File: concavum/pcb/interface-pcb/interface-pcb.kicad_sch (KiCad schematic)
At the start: 19 parts, among them J1 USB_C_Port, J2 Audio_Jack, J3 ISP_pads, J4 FPC_connector, U1 ATmega32U4-A, U2 MCP23017_SO, Y1 Crystal_16MHz

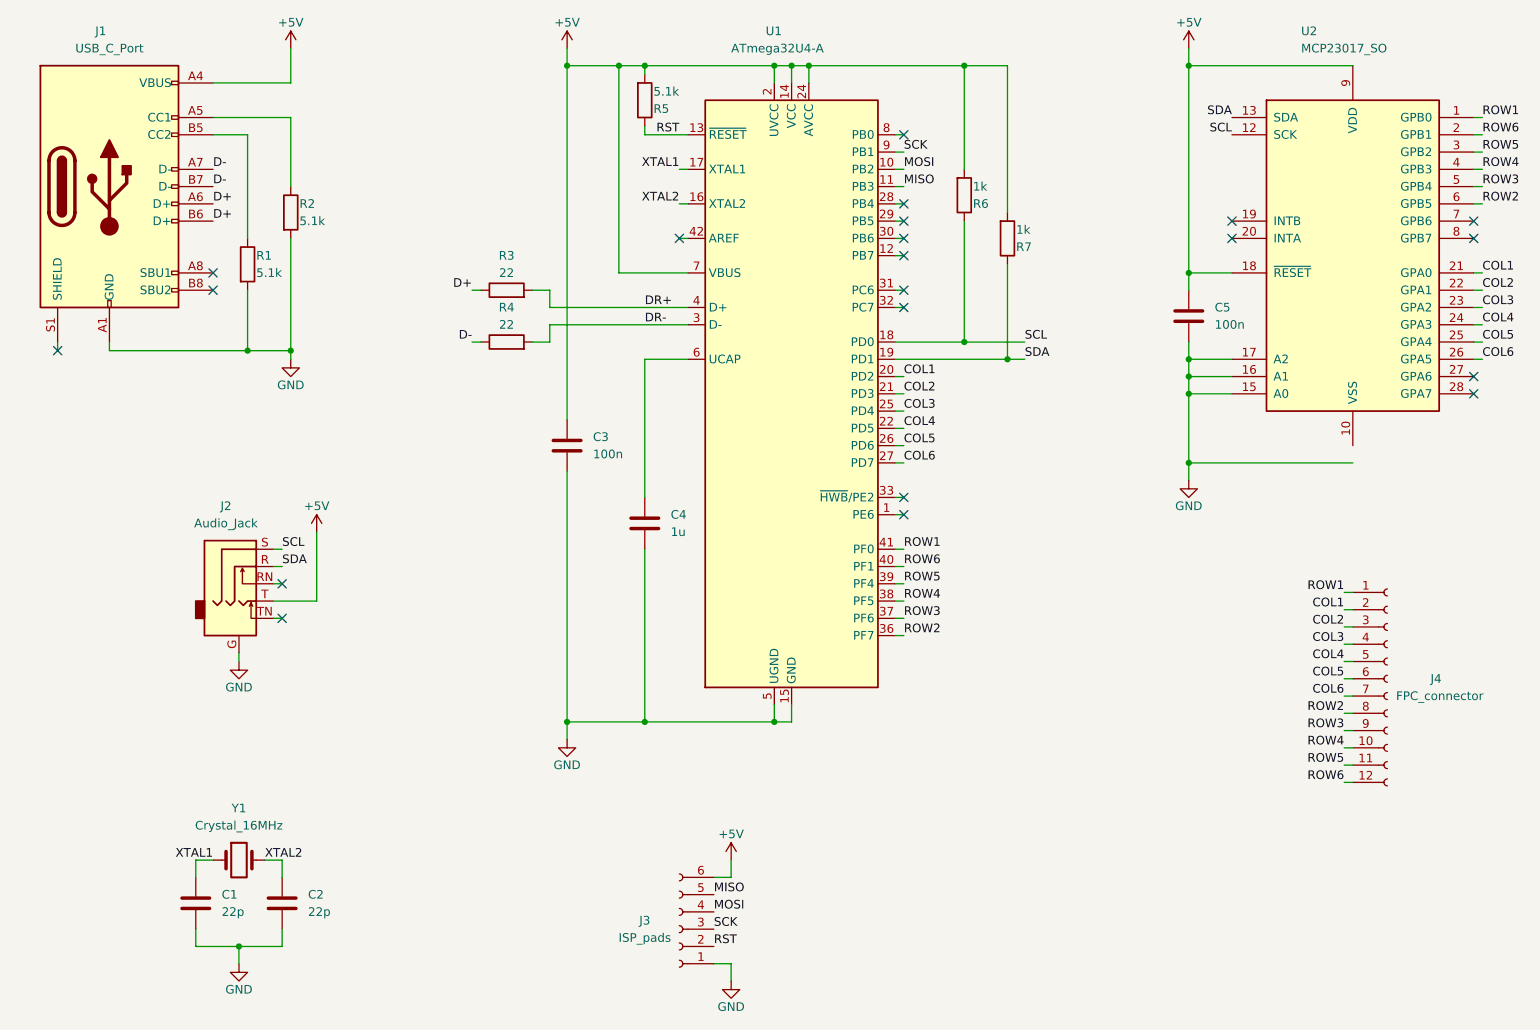
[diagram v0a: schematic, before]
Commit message: Add a 10µF capacitor as desrcibed in the datasheet
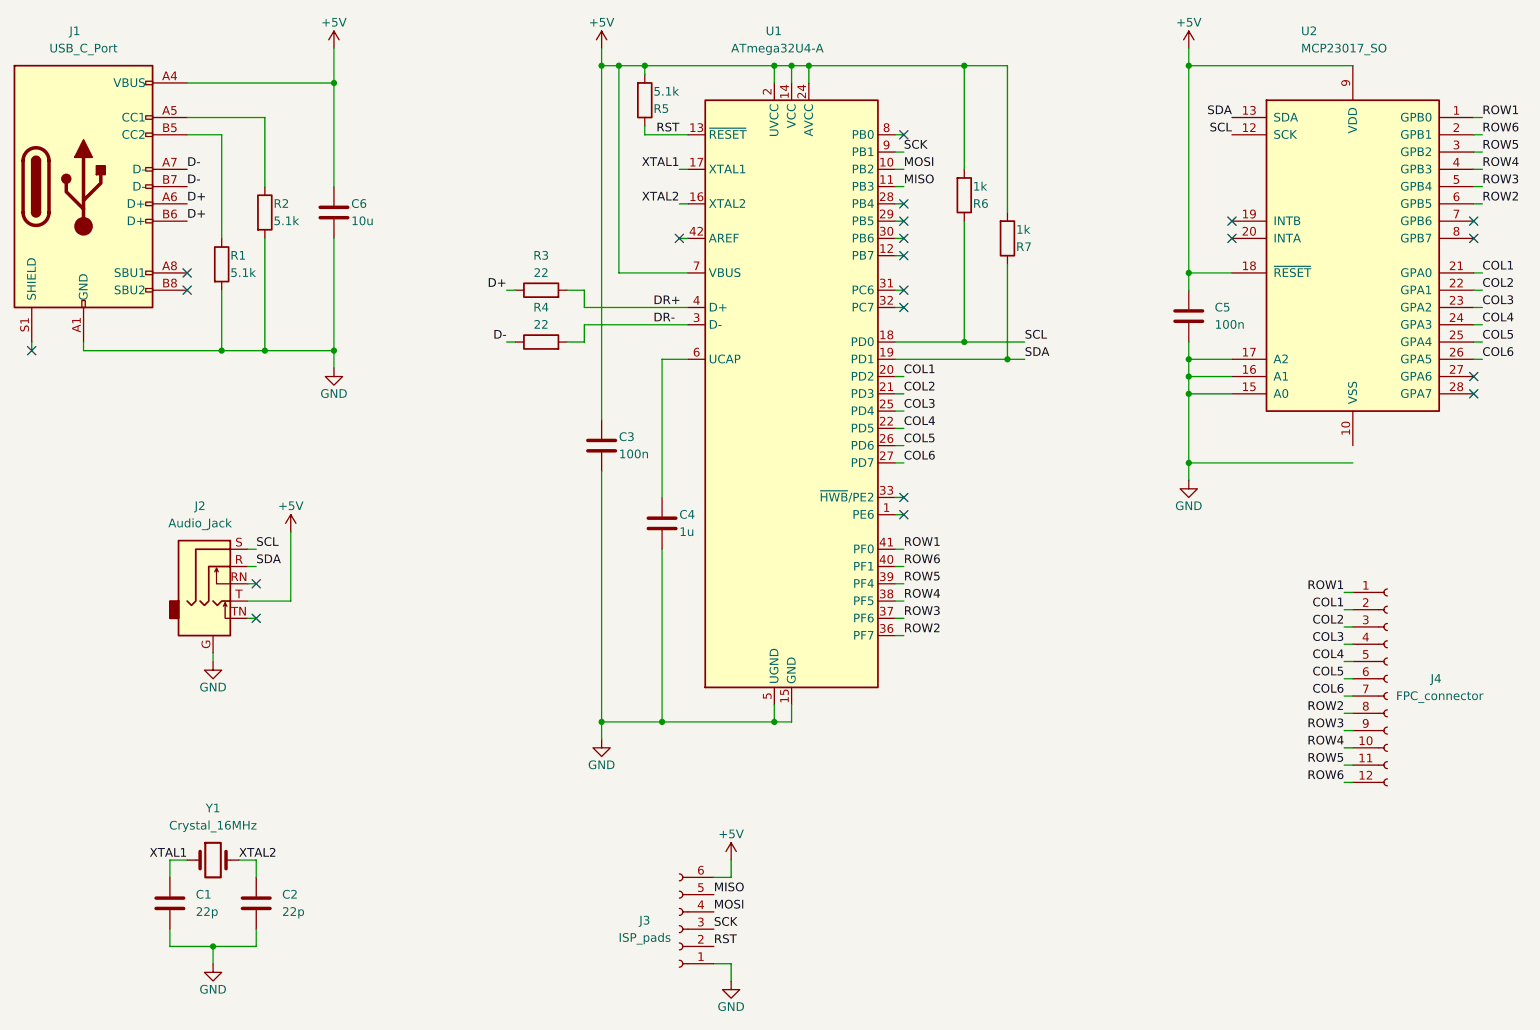
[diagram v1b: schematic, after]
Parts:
- added C6: 10u, Capacitor_SMD:C_0603_1608Metric, symbol Device:C
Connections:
- net +5V: now also C6.1
- net GND: now also C6.2
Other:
- moved on the sheet: C1, C2, C3, C4, J1, J2, R1, R2, R3, R4, Y1

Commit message: Improve footprints
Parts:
- U1: footprint Package_QFP:TQFP-44_10x10mm_P0.8mm -> Custom:TQFP-44-Rounded-Pads
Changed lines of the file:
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@@
       (effects (font (size 1.27 1.27)) (justify left))
     )
-    (property "Footprint" "Package_QFP:TQFP-44_10x10mm_P0.8mm" (id 2) (at 151.13 82.55 0)
+    (property "Footprint" "Custom:TQFP-44-Rounded-Pads" (id 2) (at 151.13 82.55 0)
       (effects (font (size 1.27 1.27) italic) hide)
     )
@@
     )
     (path "/4e171e27-0952-4a5f-bd26-afc8662a6d9a"
-      (reference "U1") (unit 1) (value "ATmega32U4-A") (footprint "Package_QFP:TQFP-44_10x10mm_P0.8mm")
+      (reference "U1") (unit 1) (value "ATmega32U4-A") (footprint "Custom:TQFP-44-Rounded-Pads")
     )
     (path "/48cffc50-fb06-4eb1-9b93-78f85a43b110"

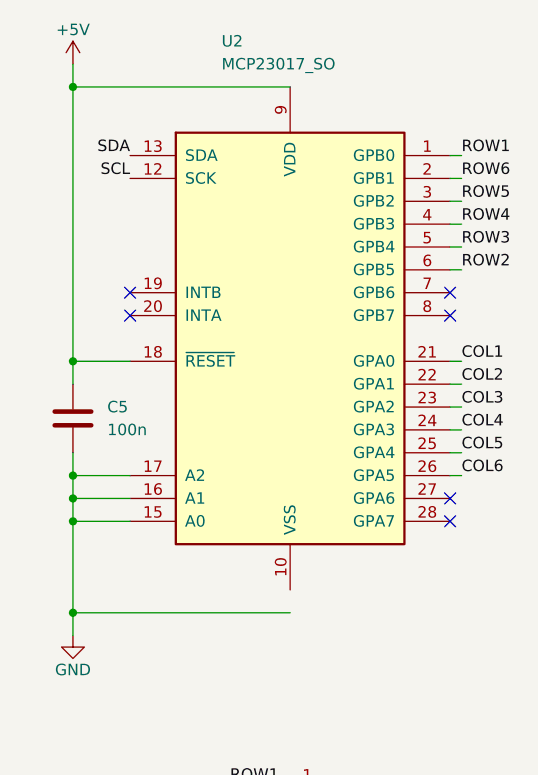
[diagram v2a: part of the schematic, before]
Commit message: Change port expander row and column pins
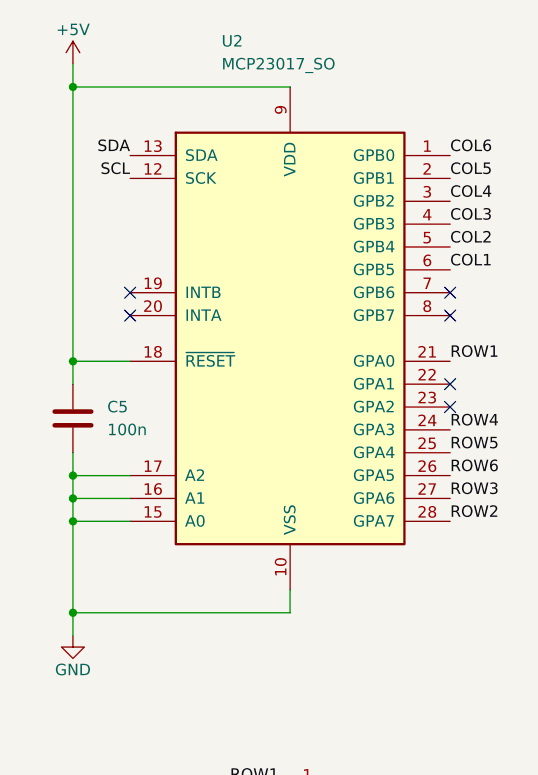
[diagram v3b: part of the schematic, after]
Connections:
- net COL1: now also U2.6 (GPB5); no longer U2.21 (GPA0)
- net COL2: now also U2.5 (GPB4); no longer U2.22 (GPA1)
- net COL3: now also U2.4 (GPB3); no longer U2.23 (GPA2)
- net COL4: now also U2.3 (GPB2); no longer U2.24 (GPA3)
- net COL5: now also U2.2 (GPB1); no longer U2.25 (GPA4)
- net COL6: now also U2.1 (GPB0); no longer U2.26 (GPA5)
- net GND: now also U2.10 (VSS)
- net ROW1: now also U2.21 (GPA0); no longer U2.1 (GPB0)
- net ROW2: now also U2.28 (GPA7); no longer U2.6 (GPB5)
- net ROW3: now also U2.27 (GPA6); no longer U2.5 (GPB4)
- net ROW4: now also U2.24 (GPA3); no longer U2.4 (GPB3)
- net ROW5: now also U2.25 (GPA4); no longer U2.3 (GPB2)
- net ROW6: now also U2.26 (GPA5); no longer U2.2 (GPB1)
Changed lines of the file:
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@@
   (no_connect (at 72.39 110.49))
   (no_connect (at 72.39 115.57))
-  (no_connect (at 251.46 82.55))
+  (no_connect (at 251.46 59.69))
   (no_connect (at 251.46 57.15))
-  (no_connect (at 251.46 59.69))
-  (no_connect (at 251.46 80.01))
   (no_connect (at 167.64 44.45))
   (no_connect (at 167.64 69.85))
@@
   (no_connect (at 39.37 76.2))
   (no_connect (at 134.62 59.69))
+  (no_connect (at 251.46 69.85))
+  (no_connect (at 251.46 67.31))
   (no_connect (at 215.9 57.15))
   (no_connect (at 215.9 59.69))
@@
     (stroke (width 0) (type default) (color 0 0 0 0))
   )
-  (wire (pts (xy 251.46 74.93) (xy 252.73 74.93))
-    (stroke (width 0) (type default) (color 0 0 0 0))
-  )
   (wire (pts (xy 182.88 55.88) (xy 182.88 34.29))
     (stroke (width 0) (type default) (color 0 0 0 0))
@@
     (stroke (width 0) (type default) (color 0 0 0 0))
   )
-  (wire (pts (xy 252.73 52.07) (xy 251.46 52.07))
-    (stroke (width 0) (type default) (color 0 0 0 0))
-  )
   (wire (pts (xy 166.37 92.71) (xy 167.64 92.71))
     (stroke (width 0) (type default) (color 0 0 0 0))
@@
     (stroke (width 0) (type default) (color 0 0 0 0))
   )
-  (wire (pts (xy 251.46 72.39) (xy 252.73 72.39))
-    (stroke (width 0) (type default) (color 0 0 0 0))
-  )
   (wire (pts (xy 120.65 74.93) (xy 120.65 72.39))
     (stroke (width 0) (type default) (color 0 0 0 0))
@@
     (stroke (width 0) (type default) (color 0 0 0 0))
   )
-  (wire (pts (xy 252.73 54.61) (xy 251.46 54.61))
-    (stroke (width 0) (type default) (color 0 0 0 0))
-  )
   (wire (pts (xy 167.64 118.11) (xy 166.37 118.11))
     (stroke (width 0) (type default) (color 0 0 0 0))
@@
     (stroke (width 0) (type default) (color 0 0 0 0))
   )
-  (wire (pts (xy 252.73 49.53) (xy 251.46 49.53))
-    (stroke (width 0) (type default) (color 0 0 0 0))
-  )
   (wire (pts (xy 166.37 90.17) (xy 167.64 90.17))
     (stroke (width 0) (type default) (color 0 0 0 0))
   )
-  (wire (pts (xy 251.46 77.47) (xy 252.73 77.47))
-    (stroke (width 0) (type default) (color 0 0 0 0))
-  )
   (wire (pts (xy 166.37 97.79) (xy 167.64 97.79))
     (stroke (width 0) (type default) (color 0 0 0 0))
@@
     (stroke (width 0) (type default) (color 0 0 0 0))
   )
-  (wire (pts (xy 252.73 46.99) (xy 251.46 46.99))
+  (wire (pts (xy 233.68 90.17) (xy 233.68 92.71))
     (stroke (width 0) (type default) (color 0 0 0 0))
   )
@@
     (stroke (width 0) (type default) (color 0 0 0 0))
   )
-  (wire (pts (xy 252.73 41.91) (xy 251.46 41.91))
-    (stroke (width 0) (type default) (color 0 0 0 0))
-  )
   (wire (pts (xy 71.12 113.03) (xy 77.47 113.03))
     (stroke (width 0) (type default) (color 0 0 0 0))
   )
-  (wire (pts (xy 252.73 44.45) (xy 251.46 44.45))
-    (stroke (width 0) (type default) (color 0 0 0 0))
-  )
   (wire (pts (xy 232.41 139.7) (xy 233.68 139.7))
     (stroke (width 0) (type default) (color 0 0 0 0))
@@
     (stroke (width 0) (type default) (color 0 0 0 0))
   )
-  (wire (pts (xy 251.46 69.85) (xy 252.73 69.85))
-    (stroke (width 0) (type default) (color 0 0 0 0))
-  )
   (wire (pts (xy 120.65 69.85) (xy 120.65 67.31))
     (stroke (width 0) (type default) (color 0 0 0 0))
@@
     (stroke (width 0) (type default) (color 0 0 0 0))
   )
-  (wire (pts (xy 251.46 64.77) (xy 252.73 64.77))
-    (stroke (width 0) (type default) (color 0 0 0 0))
-  )
   (wire (pts (xy 83.82 59.69) (xy 83.82 76.2))
     (stroke (width 0) (type default) (color 0 0 0 0))
@@
     (stroke (width 0) (type default) (color 0 0 0 0))
   )
-  (wire (pts (xy 251.46 67.31) (xy 252.73 67.31))
-    (stroke (width 0) (type default) (color 0 0 0 0))
-  )
   (wire (pts (xy 134.62 59.69) (xy 135.89 59.69))
     (stroke (width 0) (type default) (color 0 0 0 0))
@@
     (effects (font (size 1.27 1.27)) (justify left bottom))
   )
-  (label "COL3" (at 252.73 69.85 0)
+  (label "COL3" (at 251.46 49.53 0)
     (effects (font (size 1.27 1.27)) (justify left bottom))
   )
@@
     (effects (font (size 1.27 1.27)) (justify right bottom))
   )
-  (label "ROW6" (at 252.73 44.45 0)
+  (label "ROW6" (at 251.46 77.47 0)
     (effects (font (size 1.27 1.27)) (justify left bottom))
   )
@@
     (effects (font (size 1.27 1.27)) (justify left bottom))
   )
-  (label "COL2" (at 252.73 67.31 0)
+  (label "COL2" (at 251.46 52.07 0)
     (effects (font (size 1.27 1.27)) (justify left bottom))
   )
@@
     (effects (font (size 1.27 1.27)) (justify left bottom))
   )
-  (label "ROW1" (at 252.73 41.91 0)
+  (label "ROW1" (at 251.46 64.77 0)
     (effects (font (size 1.27 1.27)) (justify left bottom))
   )
@@
     (effects (font (size 1.27 1.27)) (justify left bottom))
   )
-  (label "COL6" (at 252.73 77.47 0)
+  (label "COL6" (at 251.46 41.91 0)
     (effects (font (size 1.27 1.27)) (justify left bottom))
   )
@@
     (effects (font (size 1.27 1.27)) (justify left bottom))
   )
-  (label "COL5" (at 252.73 74.93 0)
+  (label "COL5" (at 251.46 44.45 0)
     (effects (font (size 1.27 1.27)) (justify left bottom))
   )
@@
     (effects (font (size 1.27 1.27)) (justify left bottom))
   )
-  (label "ROW3" (at 252.73 52.07 0)
+  (label "ROW3" (at 251.46 80.01 0)
     (effects (font (size 1.27 1.27)) (justify left bottom))
   )
@@
     (effects (font (size 1.27 1.27)) (justify left bottom))
   )
-  (label "COL1" (at 252.73 64.77 0)
-    (effects (font (size 1.27 1.27)) (justify left bottom))
-  )
-  (label "ROW5" (at 252.73 46.99 0)
-    (effects (font (size 1.27 1.27)) (justify left bottom))
-  )
-  (label "COL4" (at 252.73 72.39 0)
+  (label "COL1" (at 251.46 54.61 0)
+    (effects (font (size 1.27 1.27)) (justify left bottom))
+  )
+  (label "ROW5" (at 251.46 74.93 0)
+    (effects (font (size 1.27 1.27)) (justify left bottom))
+  )
+  (label "COL4" (at 251.46 46.99 0)
     (effects (font (size 1.27 1.27)) (justify left bottom))
   )
@@
     (effects (font (size 1.27 1.27)) (justify left bottom))
   )
-  (label "ROW4" (at 252.73 49.53 0)
-    (effects (font (size 1.27 1.27)) (justify left bottom))
-  )
-  (label "ROW2" (at 252.73 54.61 0)
-    (effects (font (size 1.27 1.27)) (justify left bottom))
-  )
+  (label "ROW4" (at 251.46 72.39 0)
+    (effects (font (size 1.27 1.27)) (justify left bottom))
+  )
+  (label "ROW2" (at 251.46 82.55 0)
+    (effects (font (size 1.27 1.27)) (justify left bottom))
+  )

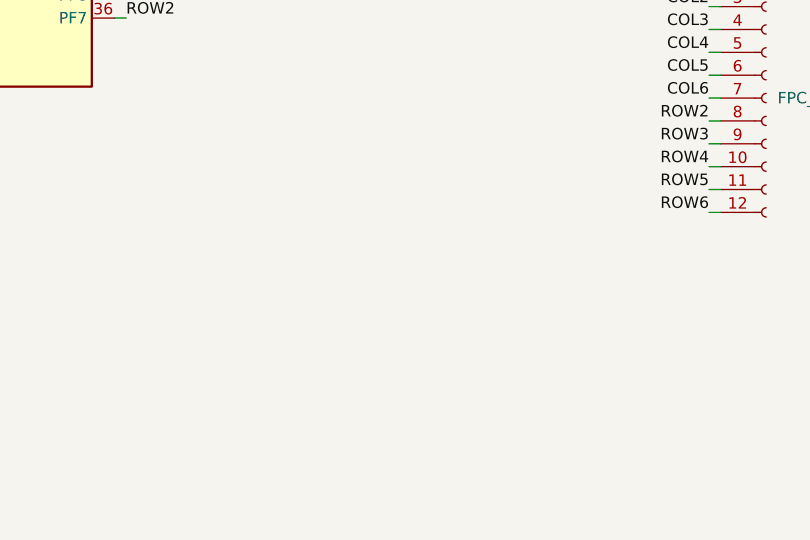
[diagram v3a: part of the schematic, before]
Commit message: Add M2 mounting holes
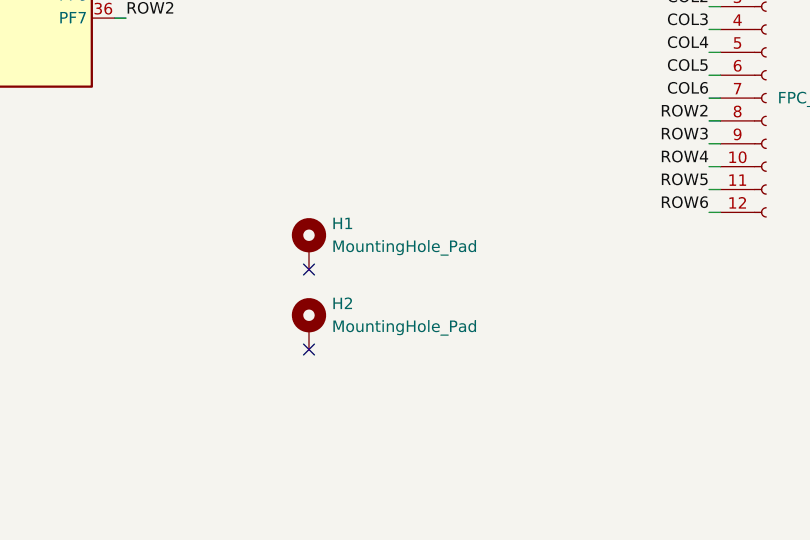
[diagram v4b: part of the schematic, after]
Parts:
- added H1, H2: MountingHole_Pad, MountingHole:MountingHole_2.2mm_M2_Pad_Via, symbol Mechanical:MountingHole_Pad
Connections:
- no-connect marks 21 -> 23
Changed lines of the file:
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@@
   (no_connect (at 215.9 57.15))
   (no_connect (at 215.9 59.69))
+  (no_connect (at 187.96 146.05))
+  (no_connect (at 187.96 154.94))
   (no_connect (at 62.23 64.77))
   (no_connect (at 62.23 67.31))
@@
     (pin "2")
   )
+  (symbol (lib_id "Mechanical:MountingHole_Pad") (at 187.96 152.4 0) (unit 1)
+    (in_bom yes) (on_board yes) (fields_autoplaced)
+    (property "Reference" "H2" (id 0) (at 190.5 149.8599 0)
+      (effects (font (size 1.27 1.27)) (justify left))
+    )
+    (property "Value" "MountingHole_Pad" (id 1) (at 190.5 152.3999 0)
+      (effects (font (size 1.27 1.27)) (justify left))
+    )
+    (property "Footprint" "MountingHole:MountingHole_2.2mm_M2_Pad_Via" (id 2) (at 187.96 152.4 0)
+      (effects (font (size 1.27 1.27)) hide)
+    )
+    (property "Datasheet" "~" (id 3) (at 187.96 152.4 0)
+      (effects (font (size 1.27 1.27)) hide)
+    )
+    (pin "1")
+  )
   (symbol (lib_id "Device:C") (at 132.08 101.6 0) (unit 1)
     (in_bom yes) (on_board yes)
@@
     (pin "1")
   )
+  (symbol (lib_id "Mechanical:MountingHole_Pad") (at 187.96 143.51 0) (unit 1)
+    (in_bom yes) (on_board yes) (fields_autoplaced)
+    (property "Reference" "H1" (id 0) (at 190.5 140.9699 0)
+      (effects (font (size 1.27 1.27)) (justify left))
+    )
+    (property "Value" "MountingHole_Pad" (id 1) (at 190.5 143.5099 0)
+      (effects (font (size 1.27 1.27)) (justify left))
+    )
+    (property "Footprint" "MountingHole:MountingHole_2.2mm_M2_Pad_Via" (id 2) (at 187.96 143.51 0)
+      (effects (font (size 1.27 1.27)) hide)
+    )
+    (property "Datasheet" "~" (id 3) (at 187.96 143.51 0)
+      (effects (font (size 1.27 1.27)) hide)
+    )
+    (pin "1")
+  )
   (symbol (lib_id "power:GND") (at 83.82 78.74 0) (mirror y) (unit 1)
     (in_bom yes) (on_board yes)
@@
       (reference "C6") (unit 1) (value "10u") (footprint "Capacitor_SMD:C_0603_1608Metric")
     )
+    (path "/d385ebb9-fe43-4fe3-ae5a-b83665559f7f"
+      (reference "H1") (unit 1) (value "MountingHole_Pad") (footprint "MountingHole:MountingHole_2.2mm_M2_Pad_Via")
+    )
+    (path "/93c69ef9-1770-4581-b1e1-5081ba33f1fa"
+      (reference "H2") (unit 1) (value "MountingHole_Pad") (footprint "MountingHole:MountingHole_2.2mm_M2_Pad_Via")
+    )
     (path "/4792c2b5-7bb0-4ba2-b6f2-3ef1f0e802ce"
